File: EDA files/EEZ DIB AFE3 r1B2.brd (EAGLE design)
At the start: 132 x 68.5 mm, 180 parts, among them IC1 AMC3330QDWERQ1, IC10 N.C., IC11 ADS131E04IPAGR, IC12 TPS71725DCKR, IC13 TPS72325DBVR, IC2 ULN2803ADWR, IC3 AMC3301DWER, IC4 MCP6004T-I/ST, IC5 DG212BDY-T1-E3, IC6 MCP6001RT-I/OT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

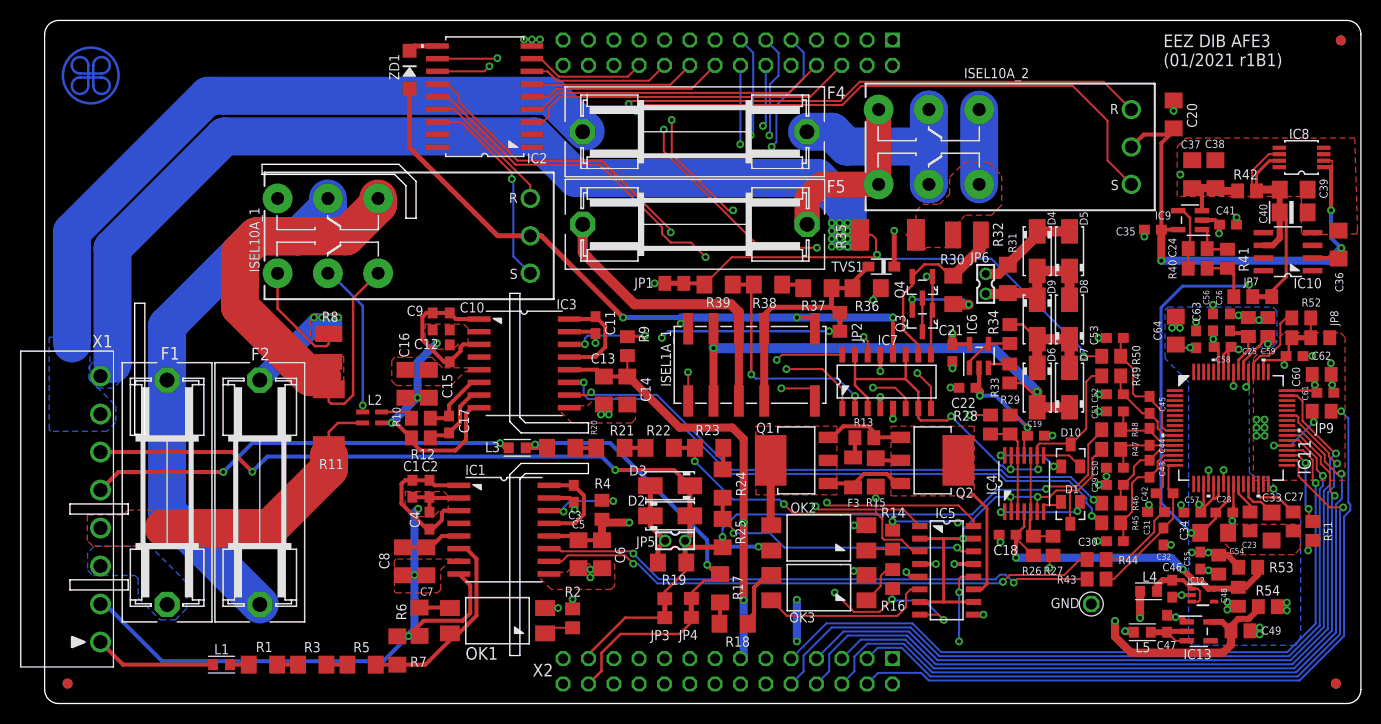
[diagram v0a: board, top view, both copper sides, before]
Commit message: r1B2 (removed RC from ADC inputs)
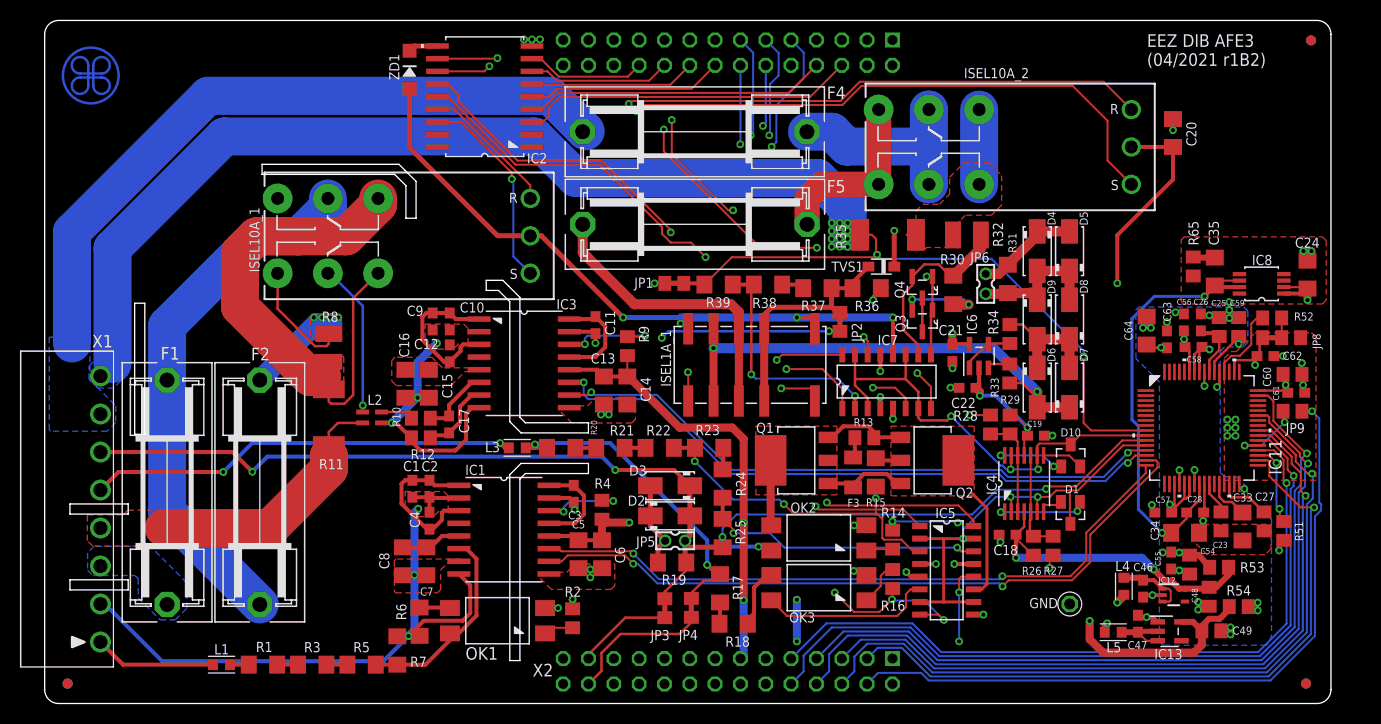
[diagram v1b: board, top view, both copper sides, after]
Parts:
- removed C29, C30, C31, C32, C50, C51, C52, C53: 470p, rcl:C0603
- removed C36, C37, C38, C39: N.C., rcl:C1206
- removed C40: N.C., EEZ_Lib1:EC1206
- removed C41: N.C., rcl:C0603
- removed C42, C43, C44, C45: 15n, rcl:C0603
- removed IC10: N.C., EEZ_TI:SOIC127P600X175-8N
- removed IC9: N.C., EEZ_TI:DBV5
- removed JP7: JP3-CUT-0805-ROTATED, EEZ_Lib1:JP3-0805-CUT2
- removed R40, R41, R42: N.C., rcl:R0805
- removed R43, R44, R45, R46, R47, R48, R49, R50: 1K, rcl:R0805
- added R65: N.C., rcl:R0805
- C24: device rcl:C0805 -> rcl:C1206
- C35: device rcl:C0603 -> rcl:C1206
- F5: value ZH32 (1A) -> ZH32 (1.25A)
- IC6: value MCP6001RT-I/OT -> MCP6001T-I/OT
- moved IC8 13.3 mm to (122.0, 41.1)
- moved C24 11.3 mm to (126.6, 42.0), turned to 90 degrees
- moved C35 7.50 mm to (117.3, 42.3), turned to 90 degrees
- moved FM2 3.00 mm to (127.0, 65.5)
- moved FM3 3.00 mm to (126.5, 1.00)
- moved C23 2.92 mm to (118.0, 17.3)
- moved C26 2.92 mm to (116.0, 37.2)
- moved C28 2.92 mm to (115.4, 18.1)
- moved C47 2.92 mm to (109.6, 7.00)
- moved C48 2.92 mm to (116.8, 9.70)
- moved C49 2.92 mm to (117.0, 6.29)
- moved C58 2.92 mm to (115.2, 34.8)
- moved C59 2.92 mm to (119.7, 36.8)
- moved C60 2.92 mm to (125.1, 32.0)
- moved C61 2.92 mm to (125.5, 30.2)
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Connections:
- removed net IN1+: C32.2, C42.2, IC11.16, R43.2
- removed net IN1-: C31.2, C42.1, IC11.15, R44.2
- removed net IN2+: C30.2, C43.2, IC11.14, R45.2
- removed net IN2-: C29.2, C43.1, IC11.13, R46.2
- removed net IN3+: C44.2, C50.2, IC11.12, R47.2
- removed net IN3-: C44.1, C51.2, IC11.11, R48.2
- removed net IN4+: C45.2, C52.2, IC11.10, R49.2
- removed net IN4-: C45.1, C53.2, IC11.9, R50.2
- removed net N$101: C37.1, C38.1, IC9.3, R42.1
- removed net N$102: C24.2, IC9.4, R40.2
- removed net N$103: C24.1, IC9.1, R41.2
- removed net N$104: JP7.NO, R40.1, R41.1
- net +5V_ISO: now also C24.1; no longer C35.1, C36.1, IC10.2, IC9.5
- net -2V5_ISO: now also C24.2; no longer C36.2, C37.2, C38.2, C39.2, C40.-, IC10.4, IC8.3, IC8.4, IC8.5, IC8.8
- net -5V_ISO: no longer C41.2, IC9.2
- net AVSS: now also IC8.3, IC8.4, IC8.5, IC8.8, R65.2
- net GND: no longer C29.1, C30.1, C31.1, C32.1, C35.2, C41.1, C50.1, C51.1, C52.1, C53.1
- net IN1N: now also IC11.15; no longer R44.1
- net IN1P: now also IC11.16; no longer R43.1
- net IN2N: now also IC11.13; no longer R46.1
- net IN2P: now also IC11.14; no longer R45.1
- net IN3N: now also IC11.11; no longer R48.1
- net IN3P: now also IC11.12; no longer R47.1
- net IN4N: now also IC11.9; no longer R50.1
- net IN4P: now also IC11.10; no longer R49.1
- net N$100: now also C35.2, R65.1; no longer C39.1, C40.+, IC10.6, IC8.6, IC8.7, JP7.NC, R42.2
- net VREFP: now also C35.1, IC8.6, IC8.7; no longer JP7.COM
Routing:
- net -5V_ISO: track 93.0 -> 42.2 mm, vias 2 -> 1
- net N$100: track 29.1 -> 2.18 mm
- net IN1+: track 16.2 -> 0.00 mm
- net IN1-: track 15.6 -> 0.00 mm
- net +5V_ISO: track 250.7 -> 236.1 mm, vias 12 -> 11
- net IN1N: track 56.4 -> 70.9 mm
- net IN4-: track 13.0 -> 0.00 mm
- net IN2+: track 12.3 -> 0.00 mm
- net IN1P: track 55.9 -> 67.9 mm
- net IN4N: track 50.8 -> 62.2 mm
- net IN4+: track 9.24 -> 0.00 mm
- net IN2-: track 9.02 -> 0.00 mm
- net GND: track 59.9 -> 51.7 mm, vias 51 -> 41
- net IN3-: track 8.07 -> 0.00 mm
- net -2V5_ISO: track 118.8 -> 126.6 mm, vias 4 -> 5
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- removed copper zone on layer 1, net -2V5_ISO
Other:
- board size 132 x 68.5 mm -> 129 x 68.5 mm
- board text added: "EEZ DIB AFE3 (04/2021 r1B2)"
- board text removed: "EEZ DIB AFE3 (01/2021 r1B1)"
